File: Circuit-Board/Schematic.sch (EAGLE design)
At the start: 17 parts, among them Q1 MOSFET-NCHANNEL2N7000, U1 DS1631U+

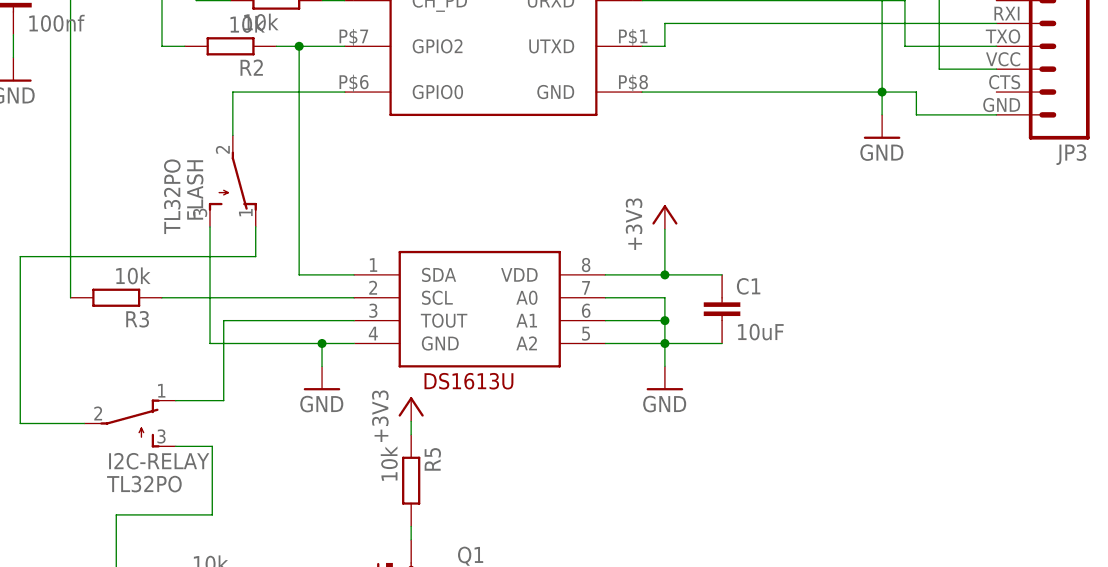
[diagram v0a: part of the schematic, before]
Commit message: Updated circuit board
Major error in circuit board design with second switch going to Tout
instead of SCK on the DS1361.
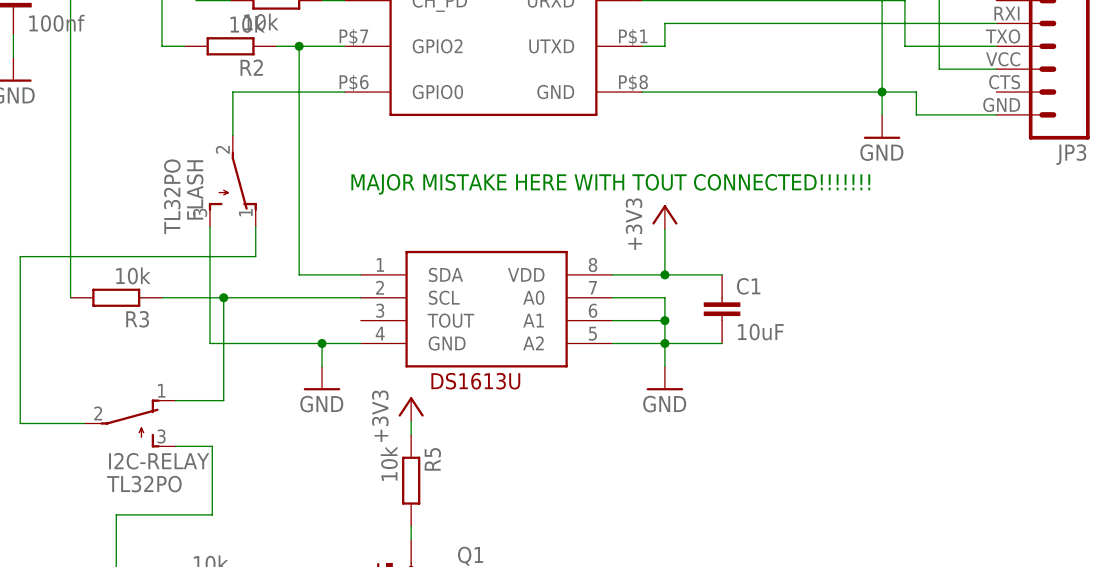
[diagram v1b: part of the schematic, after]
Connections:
- removed net N$3: R3.1, U1.SCL
- net N$9: now also R3.1, U1.SCL; no longer U1.TOUT
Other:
- note added: "MAJOR MISTAKE HERE WITH TOUT CONNECTED!!!!!!!"
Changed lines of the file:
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@@
 <sheet>
 <plain>
+<text x="56.388" y="39.878" size="1.778" layer="91">MAJOR MISTAKE HERE WITH TOUT CONNECTED!!!!!!!</text>
 </plain>
 <instances>
 <instance part="U$1" gate="G$1" x="55.88" y="50.8"/>
 <instance part="RESET" gate="G$1" x="104.14" y="66.04"/>
-<instance part="U1" gate="G$1" x="67.056" y="27.94"/>
+<instance part="U1" gate="G$1" x="67.818" y="27.94"/>
 <instance part="+3V1" gate="G$1" x="19.05" y="81.28"/>
 <instance part="+3V2" gate="G$1" x="91.44" y="38.1"/>
@@
 <pinref part="U1" gate="G$1" pin="VDD"/>
 <pinref part="+3V2" gate="G$1" pin="+3V3"/>
-<wire x1="84.836" y1="30.48" x2="91.44" y2="30.48" width="0.1524" layer="91"/>
+<wire x1="85.598" y1="30.48" x2="91.44" y2="30.48" width="0.1524" layer="91"/>
 <wire x1="91.44" y1="30.48" x2="91.44" y2="35.56" width="0.1524" layer="91"/>
 <pinref part="C1" gate="G$1" pin="1"/>
@@
 <pinref part="U1" gate="G$1" pin="GND"/>
 <pinref part="GND2" gate="1" pin="GND"/>
-<wire x1="56.896" y1="22.86" x2="53.34" y2="22.86" width="0.1524" layer="91"/>
+<wire x1="57.658" y1="22.86" x2="53.34" y2="22.86" width="0.1524" layer="91"/>
 <wire x1="53.34" y1="22.86" x2="53.34" y2="20.32" width="0.1524" layer="91"/>
 <pinref part="FLASH" gate="BEF1" pin="S"/>
@@
 <pinref part="U1" gate="G$1" pin="A2"/>
 <pinref part="GND3" gate="1" pin="GND"/>
-<wire x1="84.836" y1="22.86" x2="91.44" y2="22.86" width="0.1524" layer="91"/>
+<wire x1="85.598" y1="22.86" x2="91.44" y2="22.86" width="0.1524" layer="91"/>
 <wire x1="91.44" y1="22.86" x2="91.44" y2="20.32" width="0.1524" layer="91"/>
 <pinref part="U1" gate="G$1" pin="A1"/>
-<wire x1="84.836" y1="25.4" x2="91.44" y2="25.4" width="0.1524" layer="91"/>
+<wire x1="85.598" y1="25.4" x2="91.44" y2="25.4" width="0.1524" layer="91"/>
 <wire x1="91.44" y1="25.4" x2="91.44" y2="22.86" width="0.1524" layer="91"/>
 <junction x="91.44" y="22.86"/>
 <pinref part="U1" gate="G$1" pin="A0"/>
-<wire x1="84.836" y1="27.94" x2="91.44" y2="27.94" width="0.1524" layer="91"/>
+<wire x1="85.598" y1="27.94" x2="91.44" y2="27.94" width="0.1524" layer="91"/>
 <wire x1="91.44" y1="27.94" x2="91.44" y2="25.4" width="0.1524" layer="91"/>
 <junction x="91.44" y="25.4"/>
@@
 </segment>
 </net>
-<net name="N$3" class="0">
-<segment>
-<pinref part="U1" gate="G$1" pin="SCL"/>
-<pinref part="R3" gate="G$1" pin="1"/>
-<wire x1="35.56" y1="27.94" x2="56.896" y2="27.94" width="0.1524" layer="91"/>
-</segment>
-</net>
 <net name="N$4" class="0">
 <segment>
 <pinref part="U1" gate="G$1" pin="SDA"/>
-<wire x1="56.896" y1="30.48" x2="50.8" y2="30.48" width="0.1524" layer="91"/>
+<wire x1="57.658" y1="30.48" x2="50.8" y2="30.48" width="0.1524" layer="91"/>
 <wire x1="50.8" y1="30.48" x2="50.8" y2="55.88" width="0.1524" layer="91"/>
 <pinref part="U$1" gate="G$1" pin="GPIO2"/>
@@
 <net name="N$9" class="0">
 <segment>
-<wire x1="56.896" y1="25.4" x2="42.418" y2="25.4" width="0.1524" layer="91"/>
-<wire x1="42.418" y1="25.4" x2="42.418" y2="16.51" width="0.1524" layer="91"/>
+<wire x1="42.418" y1="27.94" x2="42.418" y2="16.51" width="0.1524" layer="91"/>
 <wire x1="42.418" y1="16.51" x2="37.084" y2="16.51" width="0.1524" layer="91"/>
 <pinref part="I2C-RELAY" gate="BEF1" pin="O"/>
-<pinref part="U1" gate="G$1" pin="TOUT"/>
-</segment>
-</net>
+<wire x1="35.56" y1="27.94" x2="42.418" y2="27.94" width="0.1524" layer="91"/>
+<pinref part="R3" gate="G$1" pin="1"/>
+<wire x1="42.418" y1="27.94" x2="57.658" y2="27.94" width="0.1524" layer="91"/>
+<junction x="42.418" y="27.94"/>
+<pinref part="U1" gate="G$1" pin="SCL"/>
+</segment>
+</net>
